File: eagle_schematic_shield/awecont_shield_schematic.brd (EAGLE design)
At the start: 53 x 44.4 mm, 13 parts, among them U1 ARDUINO_SHIELDNO_SILK

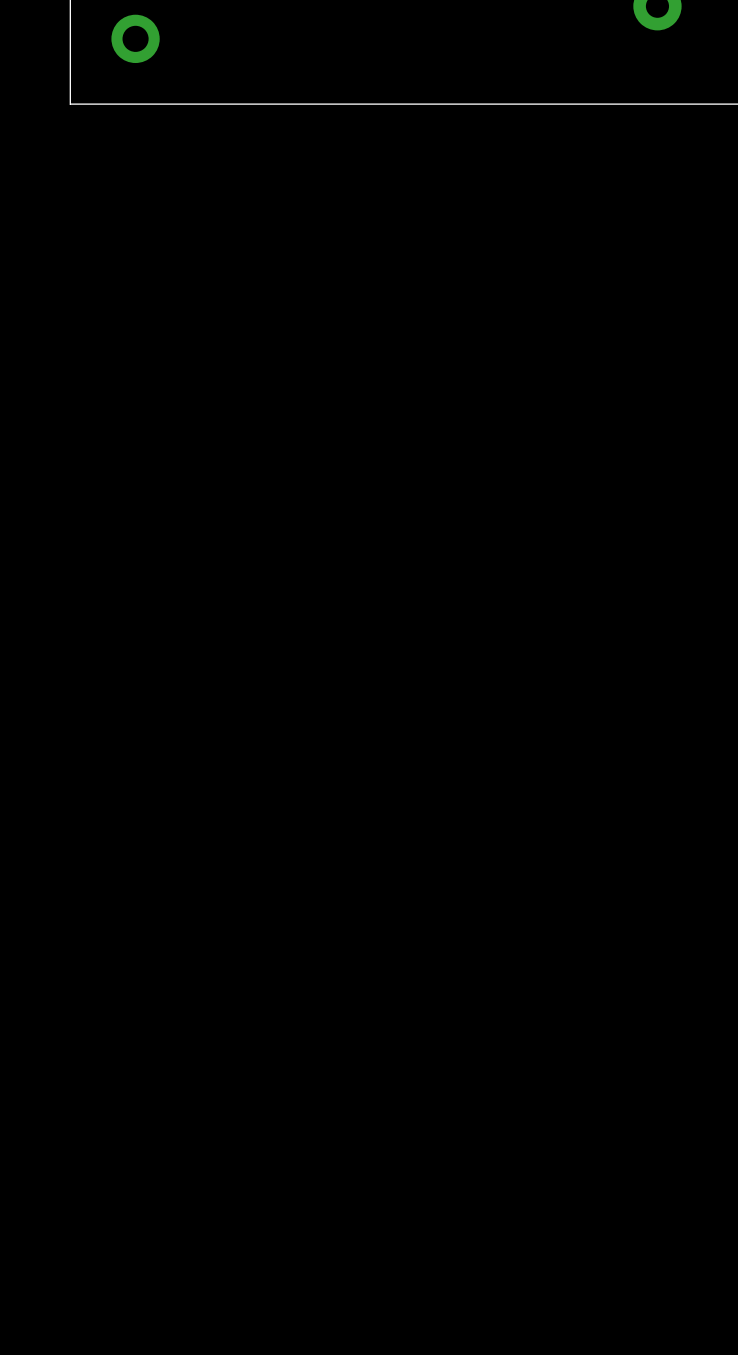
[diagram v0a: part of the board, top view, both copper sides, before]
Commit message: added dongle circuits to schematic
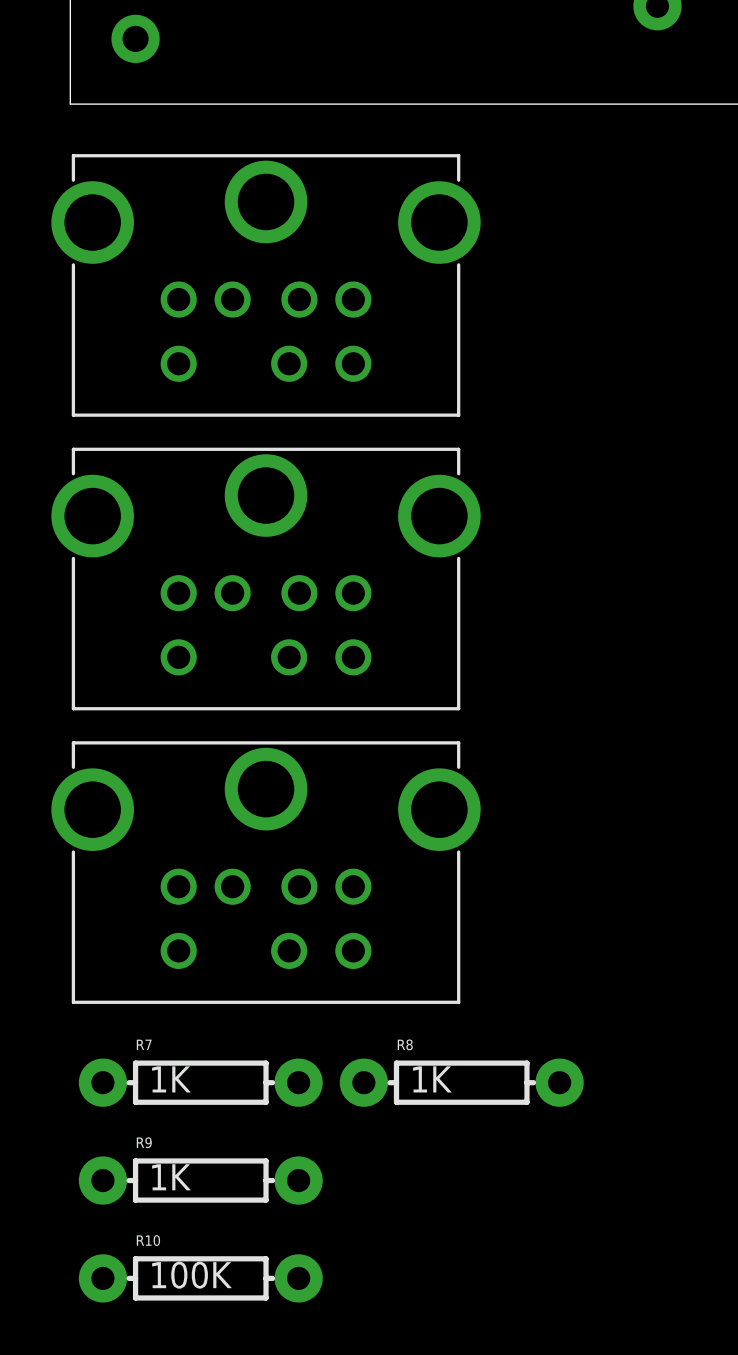
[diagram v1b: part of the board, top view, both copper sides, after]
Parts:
- added N64, NES, SNES: DIN7, SparkFun-Connectors:DIN7
- added R10: 100K, SparkFun-Passives:AXIAL-0.3
- added R7, R8, R9: 1K, SparkFun-Passives:AXIAL-0.3
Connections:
- new net CLOCK: NES.2, SNES.2
- new net DATA: N64.1, NES.1, SNES.1
- new net DETECT: R10.P$1, U1.A2
- new net LATCH: NES.3, SNES.3
- new net N$10: R8.P$1, SNES.6
- new net N$11: N64.6, R9.P$1
- new net N$17: N64.2
- new net N$19: N64.4, NES.4, SNES.4
- new net N$20: N64.5, NES.5, SNES.5
- new net N$7: NES.6, R7.P$1
- net 5V: now also R10.P$2
- net GND: now also N64.7, NES.7, R7.P$2, R8.P$2, R9.P$2, SNES.7
- net N$18: now also N64.3
- net UARTCTS: no longer U1.A2
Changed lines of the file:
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@@
 <element name="D2" library="SparkFun-LED" package="LTE-302" value="" x="34.29" y="3.81" rot="R180"/>
 <element name="R6" library="SparkFun-Passives" package="AXIAL-0.3" value="" x="43.18" y="10.16"/>
+<element name="NES" library="SparkFun-Connectors" package="DIN7" value="DIN7" x="7.62" y="-15.24"/>
+<element name="R7" library="SparkFun-Passives" package="AXIAL-0.3" value="1K" x="5.08" y="-38.1"/>
+<element name="SNES" library="SparkFun-Connectors" package="DIN7" value="DIN7" x="7.62" y="-26.67"/>
+<element name="R8" library="SparkFun-Passives" package="AXIAL-0.3" value="1K" x="15.24" y="-38.1"/>
+<element name="N64" library="SparkFun-Connectors" package="DIN7" value="DIN7" x="7.62" y="-3.81"/>
+<element name="R9" library="SparkFun-Passives" package="AXIAL-0.3" value="1K" x="5.08" y="-41.91"/>
+<element name="R10" library="SparkFun-Passives" package="AXIAL-0.3" value="100K" x="5.08" y="-45.72"/>
 </elements>
 <signals>
@@
 <contactref element="R3" pad="P$2"/>
 <contactref element="SG1" pad="-"/>
+<contactref element="R7" pad="P$2"/>
+<contactref element="NES" pad="7"/>
+<contactref element="R8" pad="P$2"/>
+<contactref element="SNES" pad="7"/>
+<contactref element="R9" pad="P$2"/>
+<contactref element="N64" pad="7"/>
 <wire x1="38.45" y1="39.21" x2="46.7" y2="39.76" width="0" layer="19" extent="1-1"/>
 <wire x1="34.85" y1="42.01" x2="38.45" y2="39.21" width="0" layer="19" extent="1-1"/>
@@
 <wire x1="10.72" y1="7.62" x2="22.86" y2="3.81" width="0" layer="19" extent="1-1"/>
 <wire x1="2.54" y1="5.08" x2="10.72" y2="7.62" width="0" layer="19" extent="1-1"/>
+<wire x1="11.02" y1="-10.11" x2="2.54" y2="5.08" width="0" layer="19" extent="1-1"/>
+<wire x1="11.02" y1="-21.54" x2="11.02" y2="-10.11" width="0" layer="19" extent="1-1"/>
+<wire x1="11.02" y1="-32.97" x2="11.02" y2="-21.54" width="0" layer="19" extent="1-1"/>
+<wire x1="8.89" y1="-38.1" x2="11.02" y2="-32.97" width="0" layer="19" extent="1-1"/>
+<wire x1="8.89" y1="-41.91" x2="8.89" y2="-38.1" width="0" layer="19" extent="1-1"/>
+<wire x1="19.05" y1="-38.1" x2="11.02" y2="-32.97" width="0" layer="19" extent="1-1"/>
 </signal>
 <signal name="N$8">
@@
 <signal name="5V">
 <contactref element="U1" pad="5V"/>
+<contactref element="R10" pad="P$2"/>
+<wire x1="8.89" y1="-45.72" x2="50.8" y2="16.51" width="0" layer="19" extent="1-1"/>
 </signal>
 <signal name="3.3V">
@@
 <contactref element="U$2" pad="16"/>
 <contactref element="R6" pad="P$2"/>
-<contactref element="U1" pad="A2"/>
-<wire x1="46.99" y1="10.16" x2="50.8" y2="34.29" width="0" layer="19" extent="1-1"/>
-<wire x1="25.05" y1="35.61" x2="50.8" y2="34.29" width="0" layer="19" extent="1-1"/>
+<wire x1="46.99" y1="10.16" x2="25.05" y2="35.61" width="0" layer="19" extent="1-1"/>
 </signal>
 <signal name="N$13">
@@
 <contactref element="R3" pad="P$1"/>
 <contactref element="R4" pad="P$2"/>
+<contactref element="N64" pad="3"/>
 <wire x1="12.7" y1="16.51" x2="20.32" y2="20.32" width="0" layer="19" extent="1-1"/>
+<wire x1="4.22" y1="-7.61" x2="12.7" y2="16.51" width="0" layer="19" extent="1-1"/>
 </signal>
 <signal name="N$1">
@@
 <wire x1="2.54" y1="24.13" x2="14.87" y2="35.61" width="0" layer="19" extent="1-1"/>
 </signal>
+<signal name="N$7">
+<contactref element="NES" pad="6"/>
+<contactref element="R7" pad="P$1"/>
+<wire x1="8.52" y1="-21.54" x2="1.27" y2="-38.1" width="0" layer="19" extent="1-1"/>
+</signal>
+<signal name="N$17">
+<contactref element="N64" pad="2"/>
+</signal>
+<signal name="N$19">
+<contactref element="NES" pad="4"/>
+<contactref element="SNES" pad="4"/>
+<contactref element="N64" pad="4"/>
+<wire x1="11.02" y1="-19.04" x2="11.02" y2="-30.47" width="0" layer="19" extent="1-1"/>
+<wire x1="11.02" y1="-7.61" x2="11.02" y2="-19.04" width="0" layer="19" extent="1-1"/>
+</signal>
+<signal name="N$20">
+<contactref element="NES" pad="5"/>
+<contactref element="SNES" pad="5"/>
+<contactref element="N64" pad="5"/>
+<wire x1="4.22" y1="-21.54" x2="4.22" y2="-32.97" width="0" layer="19" extent="1-1"/>
+<wire x1="4.22" y1="-10.11" x2="4.22" y2="-21.54" width="0" layer="19" extent="1-1"/>
+</signal>
+<signal name="N$10">
+<contactref element="SNES" pad="6"/>
+<contactref element="R8" pad="P$1"/>
+<wire x1="8.52" y1="-32.97" x2="11.43" y2="-38.1" width="0" layer="19" extent="1-1"/>
+</signal>
+<signal name="N$11">
+<contactref element="N64" pad="6"/>
+<contactref element="R9" pad="P$1"/>
+<wire x1="8.52" y1="-10.11" x2="1.27" y2="-41.91" width="0" layer="19" extent="1-1"/>
+</signal>
+<signal name="DATA">
+<contactref element="NES" pad="1"/>
+<contactref element="SNES" pad="1"/>
+<contactref element="N64" pad="1"/>
+<wire x1="8.92" y1="-19.04" x2="8.92" y2="-30.47" width="0" layer="19" extent="1-1"/>
+<wire x1="8.92" y1="-7.61" x2="8.92" y2="-19.04" width="0" layer="19" extent="1-1"/>
+</signal>
+<signal name="CLOCK">
+<contactref element="NES" pad="2"/>
+<contactref element="SNES" pad="2"/>
+<wire x1="6.32" y1="-19.04" x2="6.32" y2="-30.47" width="0" layer="19" extent="1-1"/>
+</signal>
+<signal name="LATCH">
+<contactref element="NES" pad="3"/>
+<contactref element="SNES" pad="3"/>
+<wire x1="4.22" y1="-19.04" x2="4.22" y2="-30.47" width="0" layer="19" extent="1-1"/>
+</signal>
+<signal name="DETECT">
+<contactref element="R10" pad="P$1"/>
+<contactref element="U1" pad="A2"/>
+<wire x1="1.27" y1="-45.72" x2="50.8" y2="34.29" width="0" layer="19" extent="1-1"/>
+</signal>
 </signals>

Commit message: added more detail to the schematic - mostly cleaning it up
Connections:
- removed net N$6: U$1.6, U1.D7
- net DETECT: now also U$1.6, U1.A3; no longer U1.A2
- net UARTCTS: now also U1.A2
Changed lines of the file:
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@@
 <contactref element="U$2" pad="16"/>
 <contactref element="R6" pad="P$2"/>
-<wire x1="46.99" y1="10.16" x2="25.05" y2="35.61" width="0" layer="19" extent="1-1"/>
+<contactref element="U1" pad="A2"/>
+<wire x1="46.99" y1="10.16" x2="50.8" y2="34.29" width="0" layer="19" extent="1-1"/>
+<wire x1="25.05" y1="35.61" x2="50.8" y2="34.29" width="0" layer="19" extent="1-1"/>
 </signal>
 <signal name="N$13">
@@
 <wire x1="2.54" y1="26.67" x2="10.57" y2="35.61" width="0" layer="19" extent="1-1"/>
 </signal>
-<signal name="N$6">
-<contactref element="U1" pad="D7"/>
-<contactref element="U$1" pad="6"/>
-<wire x1="2.54" y1="24.13" x2="14.87" y2="35.61" width="0" layer="19" extent="1-1"/>
-</signal>
 <signal name="N$7">
 <contactref element="NES" pad="6"/>
@@
 <signal name="DETECT">
 <contactref element="R10" pad="P$1"/>
-<contactref element="U1" pad="A2"/>
-<wire x1="1.27" y1="-45.72" x2="50.8" y2="34.29" width="0" layer="19" extent="1-1"/>
+<contactref element="U$1" pad="6"/>
+<contactref element="U1" pad="A3"/>
+<wire x1="14.87" y1="35.61" x2="50.8" y2="36.83" width="0" layer="19" extent="1-1"/>
+<wire x1="1.27" y1="-45.72" x2="14.87" y2="35.61" width="0" layer="19" extent="1-1"/>
 </signal>
 </signals>
